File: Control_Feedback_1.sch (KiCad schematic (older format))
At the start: 40 parts, among them IC3 INA818IDR, IC4 TMUX6219DGKR, IC5 TLP116A_TPL,E, IC6 TLP116A_TPL,E, IC7 ADG1402BRMZ, J1 Conn_Coaxial, J11 Conn_Coaxial, J12 Conn_Coaxial, J16 Conn_Coaxial, J7 Conn_Coaxial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

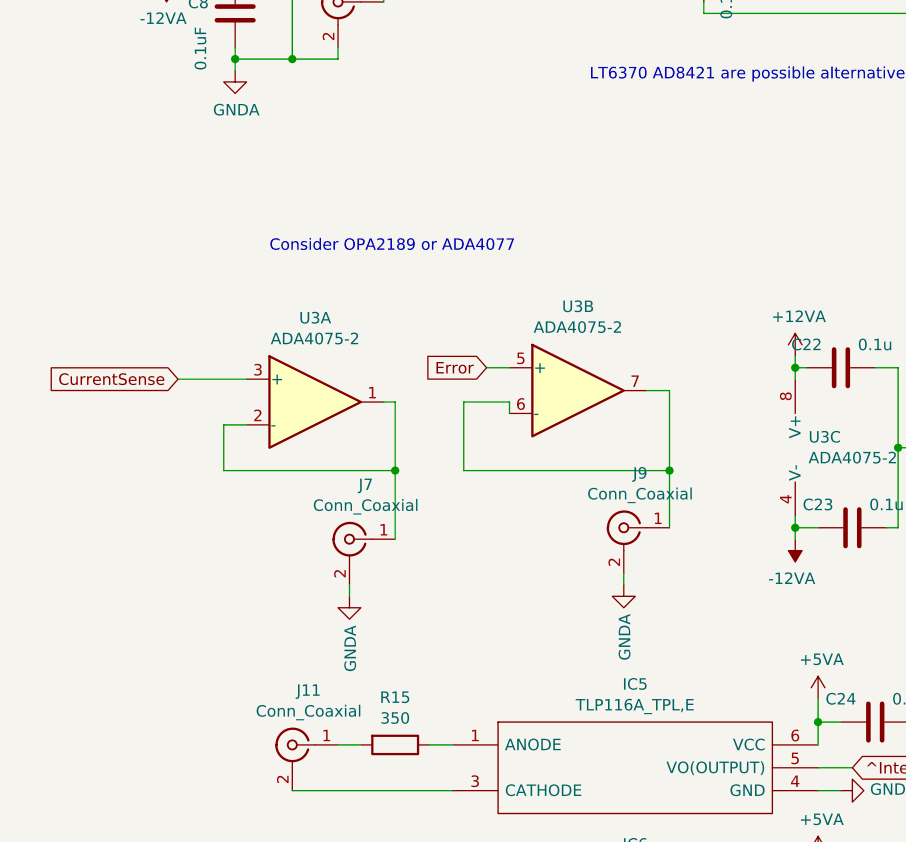
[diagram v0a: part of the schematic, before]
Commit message: Updated design, to include proper feedback and a current bias. Note the sign of the feedback might still be problematic. Need to be checked again
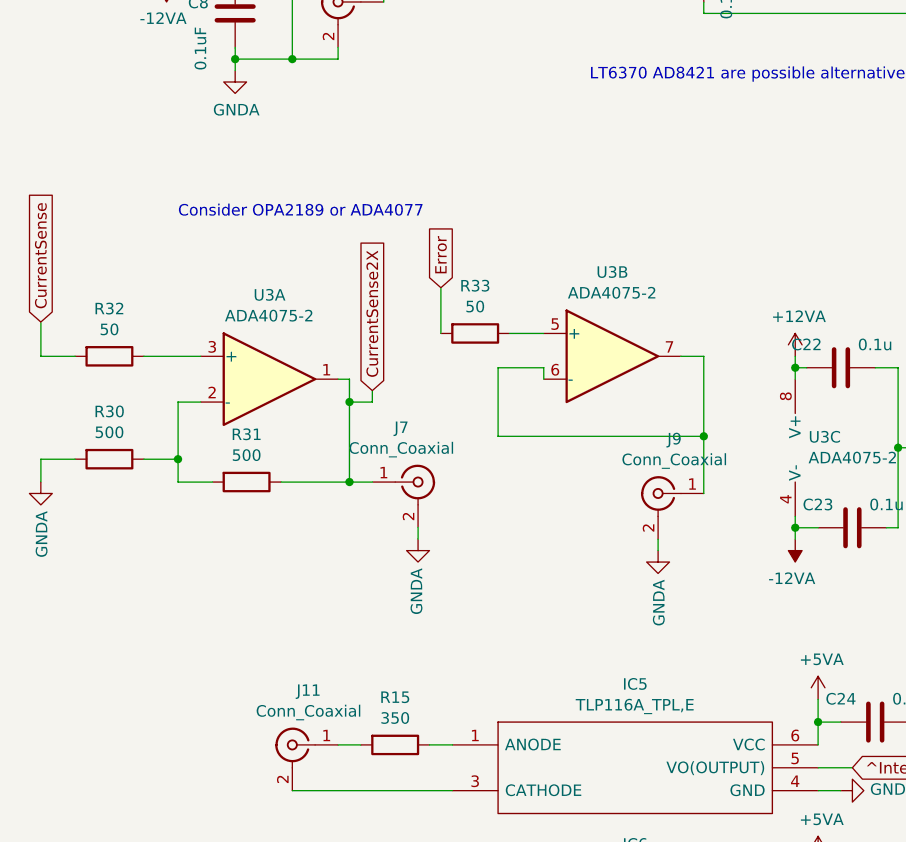
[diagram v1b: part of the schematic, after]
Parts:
- added R30, R31: 500, SamacSys_Parts:R_1206_0805_dual, symbol Device:R
- added R32, R33: 50, Resistor_SMD:R_0805_2012Metric_Pad1.15x1.40mm_HandSolder, symbol Device:R
- IC4, IC7: footprint SOP65P490X110-8N -> SamacSys_Parts:SOP65P490X110-8N
- IC5, IC6: footprint SOT127P700X230-5N -> SamacSys_Parts:SOT127P700X230-5N
- U3: footprint (none) -> Package_SO:SOIC-8_3.9x4.9mm_P1.27mm
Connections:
- net CurrentSense: now also R32.2; no longer U3.3 (+)
- net Error: now also R33.2; no longer U3.5 (+)
- net GNDA: now also R30.2
- net CurrentSense2X: now reaches J7.1 (In), U3.1
- net CurrentSense2X: now also R31.1; no longer U3.2 (-)
- new net: R30.1, R31.2, U3.2 (-)
- new net: R32.1, U3.3 (+)
- new net: R33.1, U3.5 (+)
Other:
- moved on the sheet: J7, J9, U3A, U3B
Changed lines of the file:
@@
 L Amplifier_Operational:ADA4075-2 U3
 U 1 1 60D7CC5C
-P 1850 5100
-F 0 "U3" H 1850 5467 50  0000 C CNN
-F 1 "ADA4075-2" H 1850 5376 50  0000 C CNN
-F 2 "" H 1850 5100 50  0001 C CNN
-F 3 "https://www.analog.com/static/imported-files/data_sheets/ADA4075-2.pdf" H 1850 5100 50  0001 C CNN
-	1    1850 5100
-	1    0    0    -1
-$EndComp
-Text GLabel 1250 5000 0    50   Input ~ 0
+P 1650 5000
+F 0 "U3" H 1650 5367 50  0000 C CNN
+F 1 "ADA4075-2" H 1650 5276 50  0000 C CNN
+F 2 "Package_SO:SOIC-8_3.9x4.9mm_P1.27mm" H 1650 5000 50  0001 C CNN
+F 3 "https://www.analog.com/static/imported-files/data_sheets/ADA4075-2.pdf" H 1650 5000 50  0001 C CNN
+	1    1650 5000
+	1    0    0    -1
+$EndComp
+Text GLabel 650  4750 1    50   Input ~ 0
 CurrentSense
 Wire Wire Line
-	1250 5000 1550 5000
-Wire Wire Line
-	1550 5200 1450 5200
-Wire Wire Line
-	1450 5200 1450 5400
-Wire Wire Line
-	1450 5400 2200 5400
-Wire Wire Line
-	2200 5400 2200 5100
-Wire Wire Line
-	2200 5100 2150 5100
+	1350 5100 1250 5100
+Wire Wire Line
+	2000 5000 1950 5000
 $Comp
 L Amplifier_Operational:ADA4075-2 U3
 U 2 1 60D91A0D
-P 3000 5050
-F 0 "U3" H 3000 5417 50  0000 C CNN
-F 1 "ADA4075-2" H 3000 5326 50  0000 C CNN
-F 2 "Package_SO:SOIC-8_3.9x4.9mm_P1.27mm" H 3000 5050 50  0001 C CNN
-F 3 "https://www.analog.com/static/imported-files/data_sheets/ADA4075-2.pdf" H 3000 5050 50  0001 C CNN
-	2    3000 5050
+P 3150 4900
+F 0 "U3" H 3150 5267 50  0000 C CNN
+F 1 "ADA4075-2" H 3150 5176 50  0000 C CNN
+F 2 "Package_SO:SOIC-8_3.9x4.9mm_P1.27mm" H 3150 4900 50  0001 C CNN
+F 3 "https://www.analog.com/static/imported-files/data_sheets/ADA4075-2.pdf" H 3150 4900 50  0001 C CNN
+	2    3150 4900
 	1    0    0    -1
 $EndComp
@@
 Wire Wire Line
 	5050 2600 5050 3100
-Text GLabel 2600 4950 0    50   Input ~ 0
+Text GLabel 2400 4600 1    50   Input ~ 0
 Error
 Wire Wire Line
-	2600 4950 2700 4950
-Wire Wire Line
-	3300 5050 3400 5050
-Wire Wire Line
-	3400 5400 2500 5400
-Wire Wire Line
-	2500 5400 2500 5100
-Wire Wire Line
-	2500 5100 2700 5100
-Wire Wire Line
-	2700 5100 2700 5150
+	3450 4900 3550 4900
+Wire Wire Line
+	3550 5250 2650 5250
+Wire Wire Line
+	2650 5250 2650 4950
+Wire Wire Line
+	2650 4950 2850 4950
+Wire Wire Line
+	2850 4950 2850 5000
 $Comp
 L Amplifier_Operational:ADA4075-2 U3
@@
 F 0 "U3" H 4008 5346 50  0000 L CNN
 F 1 "ADA4075-2" H 4008 5255 50  0000 L CNN
-F 2 "" H 4050 5300 50  0001 C CNN
+F 2 "Package_SO:SOIC-8_3.9x4.9mm_P1.27mm" H 4050 5300 50  0001 C CNN
 F 3 "https://www.analog.com/static/imported-files/data_sheets/ADA4075-2.pdf" H 4050 5300 50  0001 C CNN
 	3    4050 5300
@@
 L power:GNDA #PWR0117
 U 1 1 60E9B844
-P 2000 5950
-F 0 "#PWR0117" H 2000 5700 50  0001 C CNN
-F 1 "GNDA" V 2005 5823 50  0000 R CNN
-F 2 "" H 2000 5950 50  0001 C CNN
-F 3 "" H 2000 5950 50  0001 C CNN
-	1    2000 5950
-	1    0    0    -1
-$EndComp
-Connection ~ 2200 5400
-Wire Wire Line
-	2200 5400 2200 5700
+P 2300 5700
+F 0 "#PWR0117" H 2300 5450 50  0001 C CNN
+F 1 "GNDA" V 2305 5573 50  0000 R CNN
+F 2 "" H 2300 5700 50  0001 C CNN
+F 3 "" H 2300 5700 50  0001 C CNN
+	1    2300 5700
+	-1   0    0    -1
+$EndComp
 Wire Wire Line
 	4400 4950 4400 5300
@@
 Wire Wire Line
 	4400 5300 4400 5650
-Text Notes 1650 4450 0    50   ~ 0
+Text Notes 1250 4300 0    50   ~ 0
 Consider OPA2189 or ADA4077\n
 Text Notes 3050 3700 0    50   ~ 0
@@
 L Connector:Conn_Coaxial J7
 U 1 1 60B62DC3
-P 2000 5700
-F 0 "J7" H 1928 5938 50  0000 C CNN
-F 1 "Conn_Coaxial" H 1928 5847 50  0000 C CNN
-F 2 "SamacSys_Parts:Coaxial_IPX_TE_23370191-1-2" H 2000 5700 50  0001 C CNN
-F 3 " ~" H 2000 5700 50  0001 C CNN
-	1    2000 5700
-	-1   0    0    -1
-$EndComp
-Wire Wire Line
-	2000 5900 2000 5950
-Wire Wire Line
-	3400 5400 3400 5650
-Wire Wire Line
-	3400 5050 3400 5400
-Connection ~ 3400 5400
+P 2300 5450
+F 0 "J7" H 2228 5688 50  0000 C CNN
+F 1 "Conn_Coaxial" H 2228 5597 50  0000 C CNN
+F 2 "SamacSys_Parts:Coaxial_IPX_TE_23370191-1-2" H 2300 5450 50  0001 C CNN
+F 3 " ~" H 2300 5450 50  0001 C CNN
+	1    2300 5450
+	1    0    0    -1
+$EndComp
+Wire Wire Line
+	2300 5650 2300 5700
+Wire Wire Line
+	3550 5250 3550 5500
+Wire Wire Line
+	3550 4900 3550 5250
+Connection ~ 3550 5250
 Wire Wire Line
 	1950 2850 2150 2850
@@
 F 0 "IC4" H 6050 3815 50  0000 C CNN
 F 1 "TMUX6219DGKR" H 6050 3724 50  0000 C CNN
-F 2 "SOP65P490X110-8N" H 6400 3650 50  0001 L CNN
+F 2 "SamacSys_Parts:SOP65P490X110-8N" H 6400 3650 50  0001 L CNN
 F 3 "https://www.ti.com/lit/ds/symlink/tmux6219.pdf?ts=1615989354363&ref_url=https%253A%252F%252Fwww.ti.com%252Fproduct%252FTMUX6219" H 6400 3550 50  0001 L CNN
 F 4 "Analog Switch/Analog Multiplexer Single 2:1 8-Pin VSSOP T/R" H 6400 3450 50  0001 L CNN "Description"
@@
 F 0 "IC7" H 7800 5115 50  0000 C CNN
 F 1 "ADG1402BRMZ" H 7800 5024 50  0000 C CNN
-F 2 "SOP65P490X110-8N" H 8200 4950 50  0001 L CNN
+F 2 "SamacSys_Parts:SOP65P490X110-8N" H 8200 4950 50  0001 L CNN
 F 3 "" H 8200 4850 50  0001 L CNN
 F 4 "Analog Devices ADG1402BRMZ, Analogue Switch SPST NO, 12 V, 8-Pin MSOP" H 8200 4750 50  0001 L CNN "Description"
@@
 F 0 "IC5" H 3250 6865 50  0000 C CNN
 F 1 "TLP116A_TPL,E" H 3250 6774 50  0000 C CNN
-F 2 "SOT127P700X230-5N" H 3900 6700 50  0001 L CNN
+F 2 "SamacSys_Parts:SOT127P700X230-5N" H 3900 6700 50  0001 L CNN
 F 3 "https://media.digikey.com/pdf/Data%20Sheets/Toshiba%20PDFs/TLP116A.pdf" H 3900 6600 50  0001 L CNN
 F 4 "High Speed Optocouplers Pwr Suply 6V100degC Oper 5.5V 3750Vrms" H 3900 6500 50  0001 L CNN "Description"
@@
 F 0 "IC6" H 3250 7565 50  0000 C CNN
 F 1 "TLP116A_TPL,E" H 3250 7474 50  0000 C CNN
-F 2 "SOT127P700X230-5N" H 3900 7400 50  0001 L CNN
+F 2 "SamacSys_Parts:SOT127P700X230-5N" H 3900 7400 50  0001 L CNN
 F 3 "https://media.digikey.com/pdf/Data%20Sheets/Toshiba%20PDFs/TLP116A.pdf" H 3900 7300 50  0001 L CNN
 F 4 "High Speed Optocouplers Pwr Suply 6V100degC Oper 5.5V 3750Vrms" H 3900 7200 50  0001 L CNN "Description"
@@
 	7150 4450 7850 4450
 Wire Wire Line
-	3200 5850 3200 5900
+	3350 5700 3350 5750
 $Comp
 L Connector:Conn_Coaxial J9
 U 1 1 60B765BB
-P 3200 5650
-F 0 "J9" H 3128 5888 50  0000 C CNN
-F 1 "Conn_Coaxial" H 3128 5797 50  0000 C CNN
-F 2 "SamacSys_Parts:Coaxial_IPX_TE_23370191-1-2" H 3200 5650 50  0001 C CNN
-F 3 " ~" H 3200 5650 50  0001 C CNN
-	1    3200 5650
+P 3350 5500
+F 0 "J9" H 3278 5738 50  0000 C CNN
+F 1 "Conn_Coaxial" H 3278 5647 50  0000 C CNN
+F 2 "SamacSys_Parts:Coaxial_IPX_TE_23370191-1-2" H 3350 5500 50  0001 C CNN
+F 3 " ~" H 3350 5500 50  0001 C CNN
+	1    3350 5500
 	-1   0    0    -1
 $EndComp
@@
 L power:GNDA #PWR016
 U 1 1 60B765B4
-P 3200 5900
-F 0 "#PWR016" H 3200 5650 50  0001 C CNN
-F 1 "GNDA" V 3205 5773 50  0000 R CNN
-F 2 "" H 3200 5900 50  0001 C CNN
-F 3 "" H 3200 5900 50  0001 C CNN
-	1    3200 5900
+P 3350 5750
+F 0 "#PWR016" H 3350 5500 50  0001 C CNN
+F 1 "GNDA" V 3355 5623 50  0000 R CNN
+F 2 "" H 3350 5750 50  0001 C CNN
+F 3 "" H 3350 5750 50  0001 C CNN
+	1    3350 5750
 	1    0    0    -1
 $EndComp
@@
 Wire Wire Line
 	8950 3450 8950 3350
+$Comp
+L Device:R R30
+U 1 1 61371F55
+P 950 5350
+F 0 "R30" V 743 5350 50  0000 C CNN
+F 1 "500" V 834 5350 50  0000 C CNN
+F 2 "SamacSys_Parts:R_1206_0805_dual" V 880 5350 50  0001 C CNN
+F 3 "~" H 950 5350 50  0001 C CNN
+	1    950  5350
+	0    1    1    0
+$EndComp
+$Comp
+L Device:R R31
+U 1 1 6138E83D
+P 1550 5450
+F 0 "R31" V 1343 5450 50  0000 C CNN
+F 1 "500" V 1434 5450 50  0000 C CNN
+F 2 "SamacSys_Parts:R_1206_0805_dual" V 1480 5450 50  0001 C CNN
+F 3 "~" H 1550 5450 50  0001 C CNN
+	1    1550 5450
+	0    1    1    0
+$EndComp
+Wire Wire Line
+	1250 5100 1250 5350
+Wire Wire Line
+	1250 5450 1400 5450
+Wire Wire Line
+	1100 5350 1250 5350
+Connection ~ 1250 5350
+Wire Wire Line
+	1250 5350 1250 5450
+Wire Wire Line
+	800  5350 650  5350
+Wire Wire Line
+	650  5350 650  5450
+$Comp
+L power:GNDA #PWR0131
+U 1 1 613E22B5
+P 650 5450
+F 0 "#PWR0131" H 650 5200 50  0001 C CNN
+F 1 "GNDA" V 655 5323 50  0000 R CNN
+F 2 "" H 650 5450 50  0001 C CNN
+F 3 "" H 650 5450 50  0001 C CNN
+	1    650  5450
+	1    0    0    -1
+$EndComp
+Wire Wire Line
+	2000 5000 2000 5100
+Wire Wire Line
+	2000 5450 1700 5450
+Connection ~ 2000 5450
+Wire Wire Line
+	2100 5450 2000 5450
+Text GLabel 2100 5050 1    50   Input ~ 0
+CurrentSense2X
+Wire Wire Line
+	2100 5050 2100 5100
+Wire Wire Line
+	2100 5100 2000 5100
+Connection ~ 2000 5100
+Wire Wire Line
+	2000 5100 2000 5450
+$Comp
+L Device:R R32
+U 1 1 614AD73E
+P 950 4900
+F 0 "R32" V 743 4900 50  0000 C CNN
+F 1 "50" V 834 4900 50  0000 C CNN
+F 2 "Resistor_SMD:R_0805_2012Metric_Pad1.15x1.40mm_HandSolder" V 880 4900 50  0001 C CNN
+F 3 "~" H 950 4900 50  0001 C CNN
+	1    950  4900
+	0    1    1    0
+$EndComp
+Wire Wire Line
+	1350 4900 1100 4900
+Wire Wire Line
+	800  4900 650  4900
+Wire Wire Line
+	650  4900 650  4750
+$Comp
+L Device:R R33
+U 1 1 614F0644
+P 2550 4800
+F 0 "R33" V 2343 4800 50  0000 C CNN
+F 1 "50" V 2434 4800 50  0000 C CNN
+F 2 "Resistor_SMD:R_0805_2012Metric_Pad1.15x1.40mm_HandSolder" V 2480 4800 50  0001 C CNN
+F 3 "~" H 2550 4800 50  0001 C CNN
+	1    2550 4800
+	0    1    1    0
+$EndComp
+Wire Wire Line
+	2400 4600 2400 4800
+Wire Wire Line
+	2700 4800 2850 4800
 $EndSCHEMATC

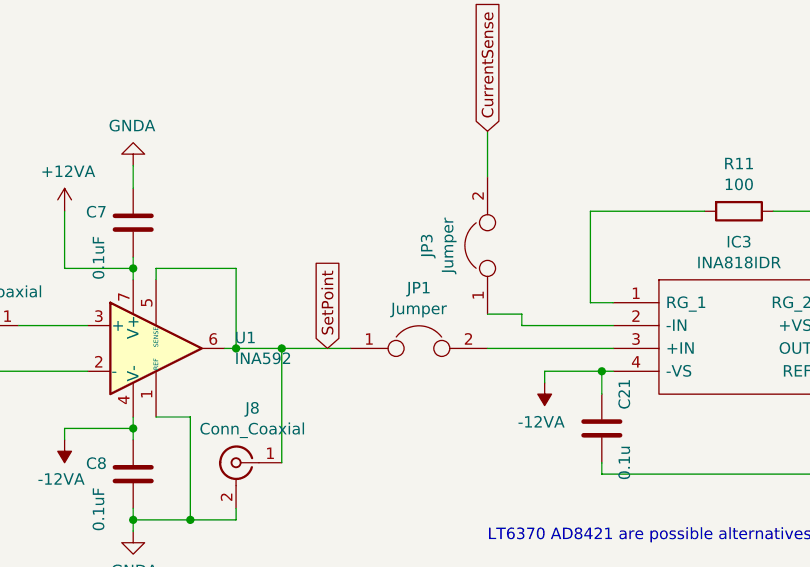
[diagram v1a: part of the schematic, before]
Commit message: Allowed swapping feedback signs
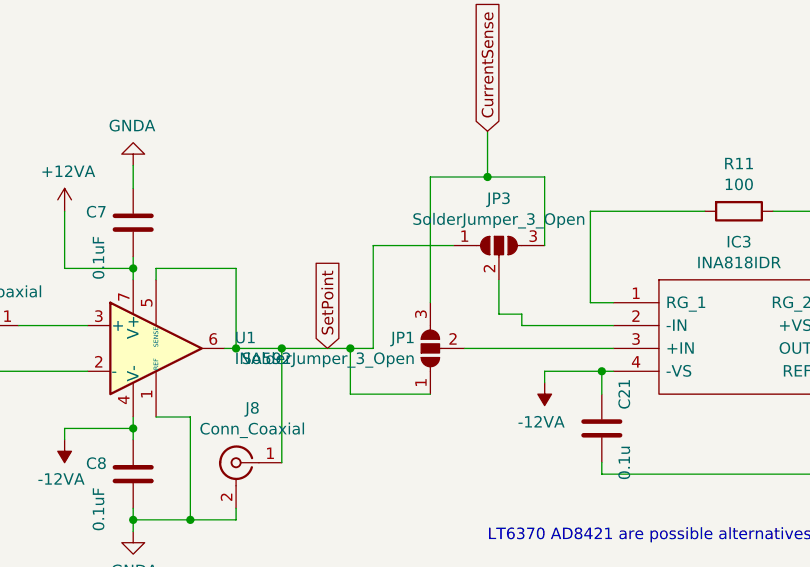
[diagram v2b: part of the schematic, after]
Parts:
- removed JP1, JP3: Jumper, Jumper:SolderJumper-2_P1.3mm_Bridged_RoundedPad1.0x1.5mm, symbol Device:Jumper
- added JP1, JP3: SolderJumper_3_Open, Jumper:SolderJumper-3_P1.3mm_Open_RoundedPad1.0x1.5mm, symbol Jumper:SolderJumper_3_Open
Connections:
- net CurrentSense: now also JP1.3 (B), JP3.3 (B)
- net SetPoint: now also JP1.1 (A), JP3.1 (A)
- net at IC3.2 (-IN): now also JP3.2 (C)
- net at IC3.3 (+IN): now also JP1.2 (C)
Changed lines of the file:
@@
 Connection ~ 1950 2850
-Wire Wire Line
-	3050 2700 3200 2700
 Wire Wire Line
 	3200 2700 3200 2750
@@
 Text Notes 3050 3700 0    50   ~ 0
 LT6370 AD8421 are possible alternatives\n
-Wire Wire Line
-	3050 2850 3600 2850
-$Comp
-L Device:Jumper JP1
-U 1 1 60EF0C1C
-P 2750 2850
-F 0 "JP1" H 2750 3114 50  0000 C CNN
-F 1 "Jumper" H 2750 3023 50  0000 C CNN
-F 2 "Jumper:SolderJumper-2_P1.3mm_Bridged_RoundedPad1.0x1.5mm" H 2750 2850 50  0001 C CNN
-F 3 "~" H 2750 2850 50  0001 C CNN
-	1    2750 2850
-	1    0    0    -1
-$EndComp
-$Comp
-L Device:Jumper JP3
-U 1 1 60F1ED0F
-P 3050 2400
-F 0 "JP3" H 3050 2664 50  0000 C CNN
-F 1 "Jumper" H 3050 2573 50  0000 C CNN
-F 2 "Jumper:SolderJumper-2_P1.3mm_Bridged_RoundedPad1.0x1.5mm" H 3050 2400 50  0001 C CNN
-F 3 "~" H 3050 2400 50  0001 C CNN
-	1    3050 2400
-	0    -1   -1   0
-$EndComp
 Wire Wire Line
 	3050 2100 3050 1900
@@
 Wire Wire Line
 	2700 4800 2850 4800
+Wire Wire Line
+	2950 2850 3600 2850
+Wire Wire Line
+	2450 2850 2450 3050
+Wire Wire Line
+	2450 3050 2800 3050
+Wire Wire Line
+	2900 2400 2550 2400
+Wire Wire Line
+	2550 2400 2550 2850
+Wire Wire Line
+	2550 2850 2450 2850
+Connection ~ 2450 2850
+Wire Wire Line
+	3300 2400 3300 2100
+Wire Wire Line
+	3300 2100 3050 2100
+Wire Wire Line
+	2800 2650 2800 2100
+Wire Wire Line
+	2800 2100 3050 2100
+Connection ~ 3050 2100
+Wire Wire Line
+	3100 2550 3100 2700
+Wire Wire Line
+	3100 2700 3200 2700
+$Comp
+L Jumper:SolderJumper_3_Open JP1
+U 1 1 6134F5AA
+P 2800 2850
+F 0 "JP1" V 2846 2917 50  0000 L CNN
+F 1 "SolderJumper_3_Open" V 2755 2917 50  0000 L CNN
+F 2 "Jumper:SolderJumper-3_P1.3mm_Open_RoundedPad1.0x1.5mm" H 2800 2850 50  0001 C CNN
+F 3 "~" H 2800 2850 50  0001 C CNN
+	1    2800 2850
+	0    -1   -1   0
+$EndComp
+$Comp
+L Jumper:SolderJumper_3_Open JP3
+U 1 1 613425C6
+P 3100 2400
+F 0 "JP3" H 3100 2605 50  0000 C CNN
+F 1 "SolderJumper_3_Open" H 3100 2514 50  0000 C CNN
+F 2 "Jumper:SolderJumper-3_P1.3mm_Open_RoundedPad1.0x1.5mm" H 3100 2400 50  0001 C CNN
+F 3 "~" H 3100 2400 50  0001 C CNN
+	1    3100 2400
+	1    0    0    -1
+$EndComp
 $EndSCHEMATC
